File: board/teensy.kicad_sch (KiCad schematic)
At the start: 0 parts

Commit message: Added Teensey
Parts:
- added U2: Teensy4.1_DEV-16771, MODULE_DEV-16771, symbol MRDT_Shields:Teensy4.1_DEV-16771
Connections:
- new net: U2.3.3V_1 (3.3V), U2.3.3V_2 (3.3V), U2.3.3V_3 (3.3V)
- new net +5V: U2.VIN
- new net GND: U2.GND1 (GND), U2.GND2 (GND), U2.GND3 (GND), U2.GND4 (GND), U2.GND5 (GND), U2.USB_GND1 (USB_GND), U2.USB_GND2 (USB_GND)

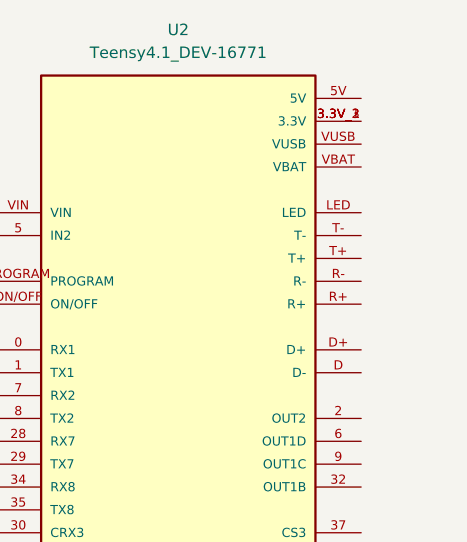
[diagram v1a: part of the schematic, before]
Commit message: Added Ethernet
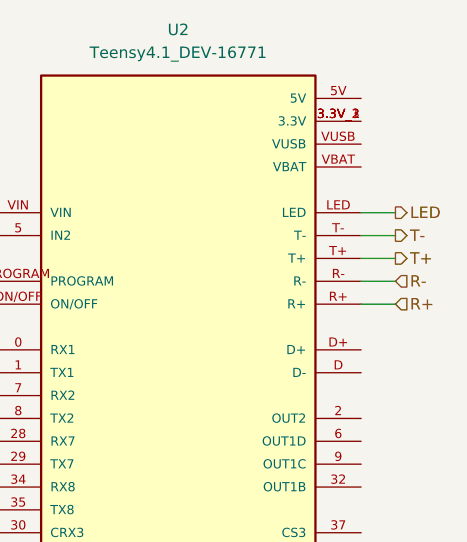
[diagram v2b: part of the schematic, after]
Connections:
- net LED: now reaches U2.LED
- net R+: now reaches U2.R+
- net R-: now reaches U2.R-
- net T+: now reaches U2.T+
- net T-: now reaches U2.T-
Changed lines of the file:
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@@
+	(wire
+		(pts
+			(xy 171.45 68.58) (xy 175.26 68.58)
+		)
+		(stroke
+			(width 0)
+			(type default)
+		)
+	)
 	(wire
 		(pts
 			(xy 125.73 66.04) (xy 130.81 66.04)
+		)
+		(stroke
+			(width 0)
+			(type default)
+		)
+	)
+	(wire
+		(pts
+			(xy 171.45 76.2) (xy 175.26 76.2)
 		)
 		(stroke
@@
 	(wire
 		(pts
+			(xy 171.45 73.66) (xy 175.26 73.66)
+		)
+		(stroke
+			(width 0)
+			(type default)
+		)
+	)
+	(wire
+		(pts
+			(xy 171.45 71.12) (xy 175.26 71.12)
+		)
+		(stroke
+			(width 0)
+			(type default)
+		)
+	)
+	(wire
+		(pts
 			(xy 177.8 152.4) (xy 177.8 149.86)
 		)
@@
 		)
 	)
+	(wire
+		(pts
+			(xy 171.45 66.04) (xy 175.26 66.04)
+		)
+		(stroke
+			(width 0)
+			(type default)
+		)
+	)
+	(hierarchical_label "T-"
+		(shape output)
+		(at 175.26 68.58 0)
+		(effects
+			(font
+				(size 1.27 1.27)
+			)
+			(justify left)
+		)
+	)
+	(hierarchical_label "LED"
+		(shape output)
+		(at 175.26 66.04 0)
+		(effects
+			(font
+				(size 1.27 1.27)
+			)
+			(justify left)
+		)
+	)
+	(hierarchical_label "R+"
+		(shape input)
+		(at 175.26 76.2 0)
+		(effects
+			(font
+				(size 1.27 1.27)
+			)
+			(justify left)
+		)
+	)
+	(hierarchical_label "R-"
+		(shape input)
+		(at 175.26 73.66 0)
+		(effects
+			(font
+				(size 1.27 1.27)
+			)
+			(justify left)
+		)
+	)
+	(hierarchical_label "T+"
+		(shape output)
+		(at 175.26 71.12 0)
+		(effects
+			(font
+				(size 1.27 1.27)
+			)
+			(justify left)
+		)
+	)

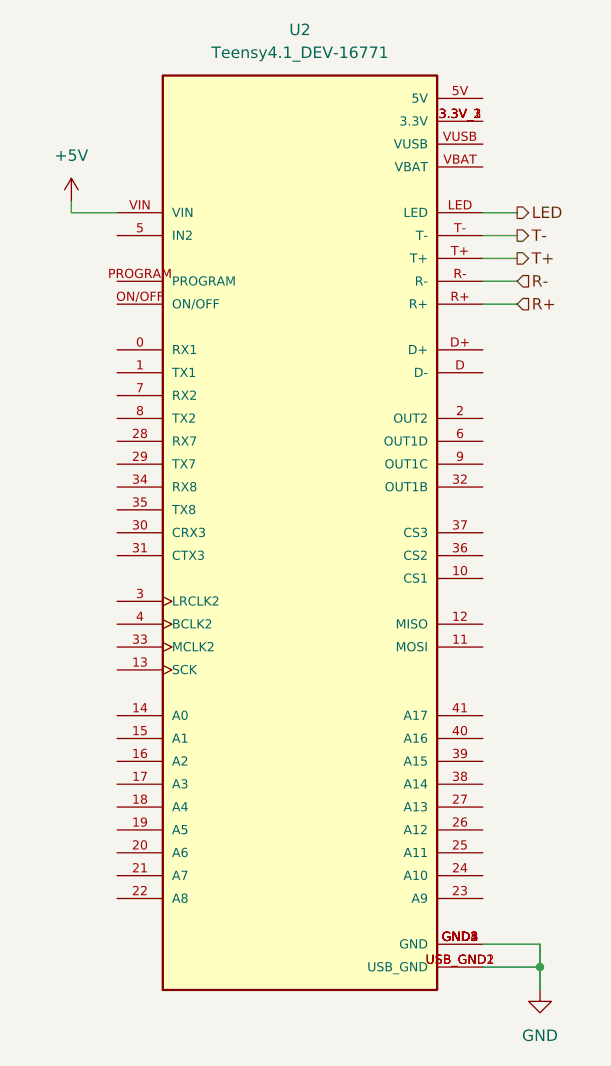
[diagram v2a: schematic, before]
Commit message: Added CAN Transceiver
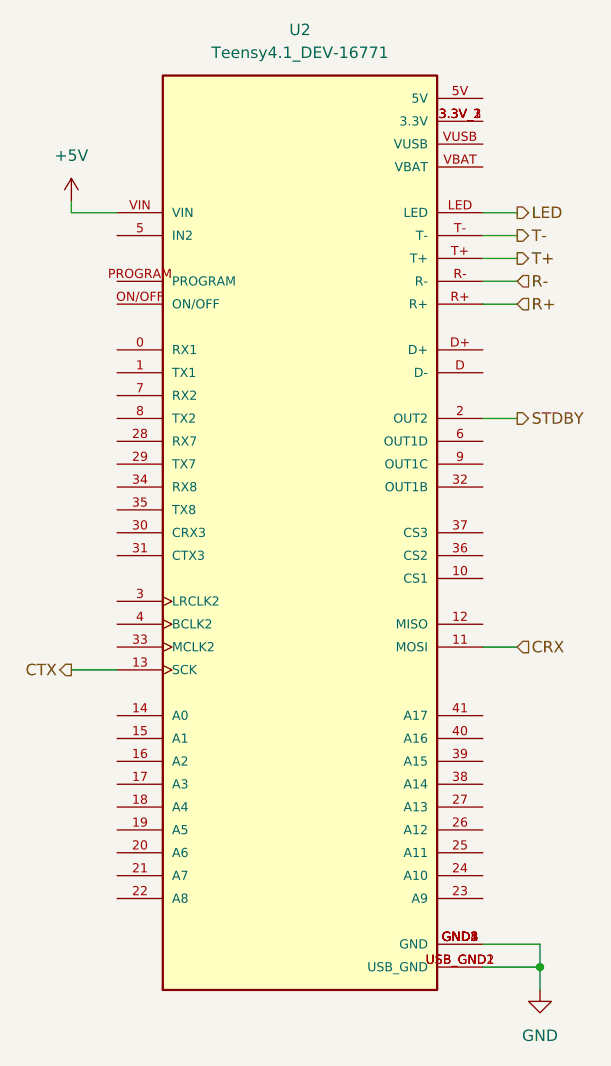
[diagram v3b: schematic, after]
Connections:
- net CRX: now reaches U2.11 (MOSI)
- net CTX: now reaches U2.13 (SCK)
- net STDBY: now reaches U2.2 (OUT2)
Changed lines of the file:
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@@
+	(wire
+		(pts
+			(xy 125.73 116.84) (xy 130.81 116.84)
+		)
+		(stroke
+			(width 0)
+			(type default)
+		)
+	)
 	(wire
 		(pts
@@
 	(wire
 		(pts
+			(xy 171.45 114.3) (xy 175.26 114.3)
+		)
+		(stroke
+			(width 0)
+			(type default)
+		)
+	)
+	(wire
+		(pts
 			(xy 177.8 147.32) (xy 177.8 149.86)
 		)
@@
 		(pts
 			(xy 171.45 71.12) (xy 175.26 71.12)
+		)
+		(stroke
+			(width 0)
+			(type default)
+		)
+	)
+	(wire
+		(pts
+			(xy 171.45 88.9) (xy 175.26 88.9)
 		)
 		(stroke
@@
 		)
 	)
+	(hierarchical_label "STDBY"
+		(shape output)
+		(at 175.26 88.9 0)
+		(effects
+			(font
+				(size 1.27 1.27)
+			)
+			(justify left)
+		)
+	)
 	(hierarchical_label "R+"
 		(shape input)
@@
 		)
 	)
+	(hierarchical_label "CRX"
+		(shape input)
+		(at 175.26 114.3 0)
+		(effects
+			(font
+				(size 1.27 1.27)
+			)
+			(justify left)
+		)
+	)
+	(hierarchical_label "CTX"
+		(shape output)
+		(at 125.73 116.84 180)
+		(effects
+			(font
+				(size 1.27 1.27)
+			)
+			(justify right)
+		)
+	)
